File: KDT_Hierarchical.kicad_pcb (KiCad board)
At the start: 2 copper layers, 34 x 40 mm, 33 parts, among them J1 22-28-8083, J2 1x3 pin vertical, J3 1x3 pin vertical, J4 1x3 pin vertical, J5 1x3 pin vertical, P1 5KEV-0, P2 5KEV-0, T1 NSI50010YT1G, U1 INA226

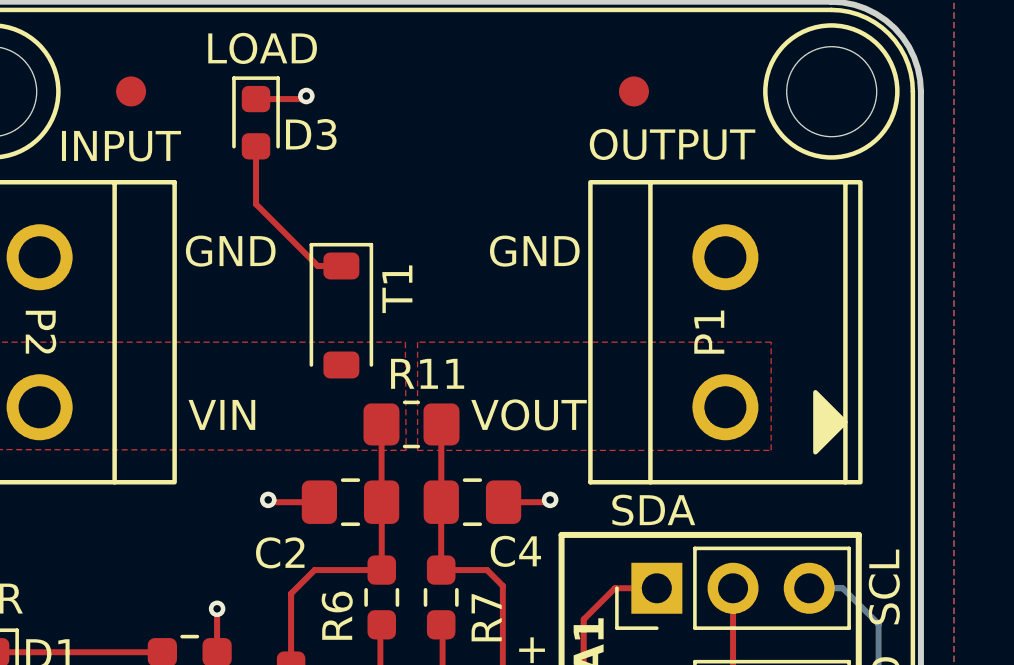
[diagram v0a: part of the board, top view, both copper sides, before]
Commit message: Changed sense resistor and fixed connector position
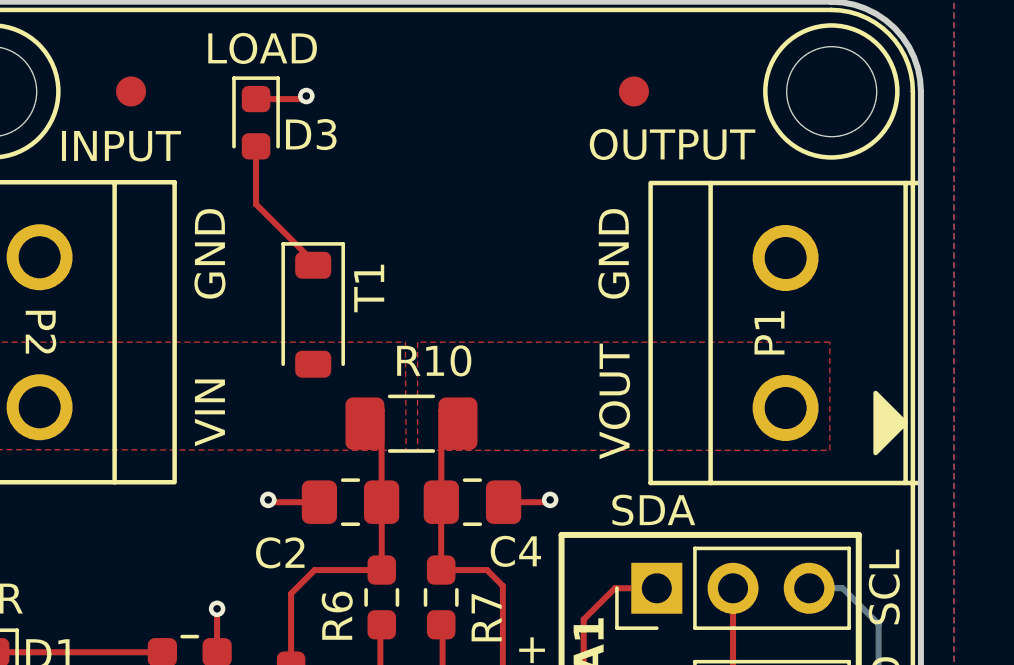
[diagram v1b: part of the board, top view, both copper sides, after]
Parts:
- removed R11: 0.002R, Resistor_SMD:R_0805_2012Metric_Pad1.20x1.40mm_HandSolder
- added R10: 0.002, Resistor_SMD:R_1206_3216Metric_Pad1.30x1.75mm_HandSolder, F.Cu at (130.5, 99.1)
- moved P1 2.01 mm to (143.0, 96.0)
- moved T1 0.94 mm to (127.2, 95.4)
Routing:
- net Net-(D3-A): track 5.63 -> 4.84 mm

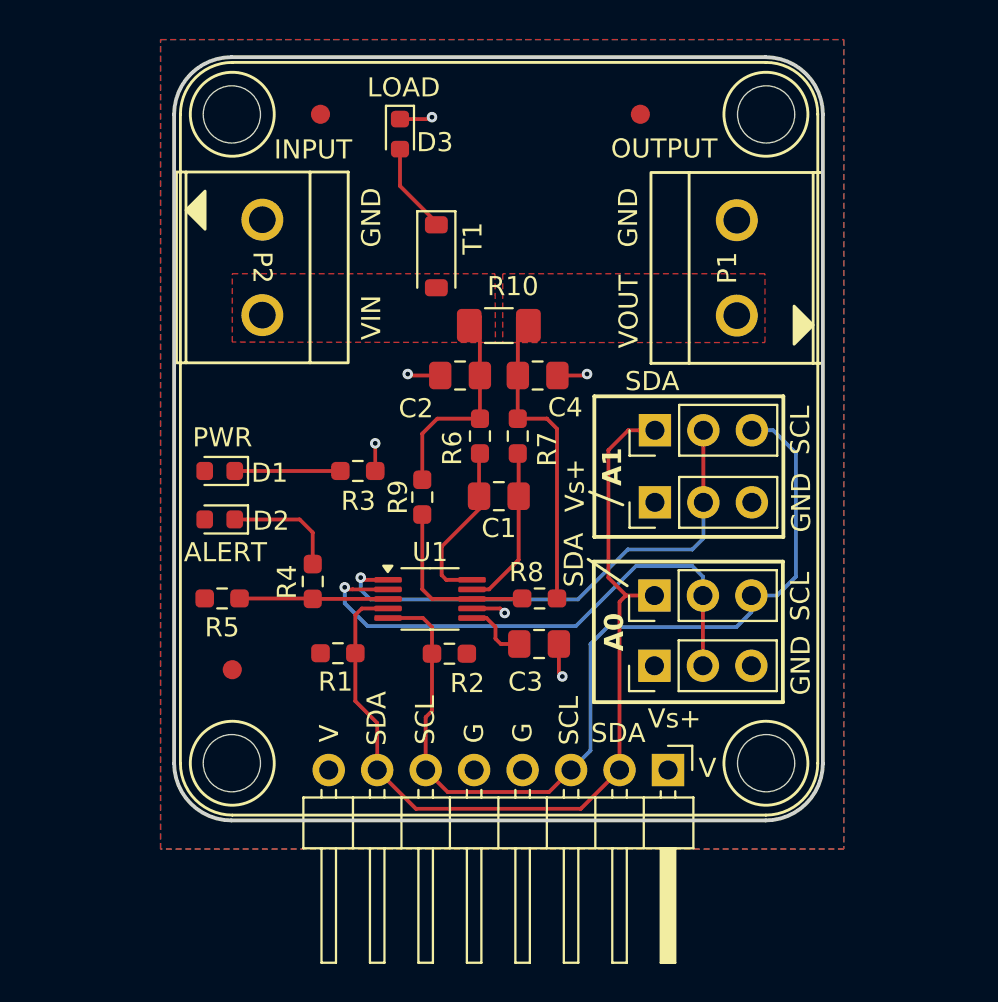
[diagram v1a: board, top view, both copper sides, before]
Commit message: Changed resistor position
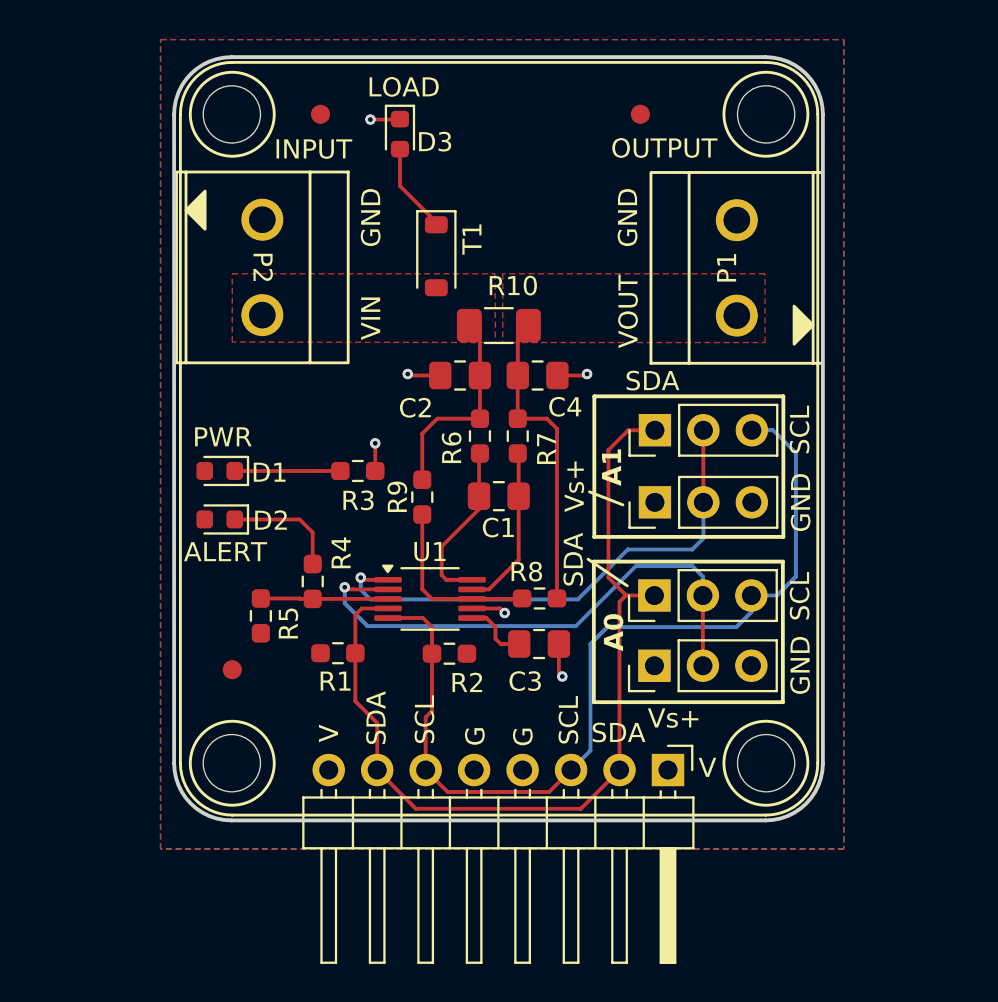
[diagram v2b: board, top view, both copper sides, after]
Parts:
- moved R5 2.23 mm to (118.0, 114.3), turned to 90 degrees
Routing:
- net /Project Architecture/Sense/ALERT: track 7.79 -> 6.71 mm
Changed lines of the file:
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@@
 		(tags "resistor handsolder")
 		(property "Reference" "R4"
-			(at 0.0254 1.3462 90)
+			(at -1.4732 -1.524 90)
 			(layer "F.SilkS")
 			(effects
@@
 	(footprint "Resistor_SMD:R_0603_1608Metric_Pad0.98x0.95mm_HandSolder"
 		(layer "F.Cu")
-		(at 116.0018 113.3602)
+		(at 118.0338 114.2746 90)
 		(descr "Resistor SMD 0603 (1608 Metric), square (rectangular) end terminal, IPC_7351 nominal with elongated pad for handsoldering. (Body size source: IPC-SM-782 page 72, https://www.pcb-3d.com/wordpress/wp-content/uploads/ipc-sm-782a_amendment_1_and_2.pdf), generated with kicad-footprint-generator")
 		(tags "resistor handsolder")
 		(property "Reference" "R5"
-			(at 0 1.524 0)
+			(at -0.4064 1.4732 90)
 			(layer "F.SilkS")
 			(effects
@@
 		)
 		(property "Value" "10K"
-			(at 0 1.43 0)
+			(at 0 1.43 90)
 			(layer "F.Fab")
 			(effects
@@
 		)
 		(property "Datasheet" "https://www.vishay.com/doc?20035"
-			(at 0 0 0)
+			(at 0 0 90)
 			(unlocked yes)
 			(layer "F.Fab")
@@
 		)
 		(property "Description" "RESISTOR, 10K, 5%, 1/10W 0603"
-			(at 0 0 0)
+			(at 0 0 90)
 			(unlocked yes)
 			(layer "F.Fab")
@@
 		)
 		(property "Sim.Device" "R"
-			(at 0 0 0)
+			(at 0 0 90)
 			(unlocked yes)
 			(layer "F.Fab")
@@
 		)
 		(property "Sim.Pins" "1=+ 2=-"
-			(at 0 0 0)
+			(at 0 0 90)
 			(unlocked yes)
 			(layer "F.Fab")
@@
 		)
 		(property "Sim.Params" "r=33"
-			(at 0 0 0)
+			(at 0 0 90)
 			(unlocked yes)
 			(layer "F.Fab")
@@
 		)
 		(property "CompanyPN" "T-RES-004"
-			(at 0 0 0)
+			(at 0 0 90)
 			(unlocked yes)
 			(layer "F.Fab")
@@
 		)
 		(property "Manufacturer Part Number" "CRCW060333R0FKEA"
-			(at 0 0 0)
+			(at 0 0 90)
 			(unlocked yes)
 			(layer "F.Fab")
@@
 		)
 		(fp_line
-			(start -1.65 -0.73)
-			(end 1.65 -0.73)
+			(start 1.65 -0.73)
+			(end 1.65 0.73)
 			(stroke
 				(width 0.05)
@@
 		)
 		(fp_line
-			(start -1.65 0.73)
-			(end -1.65 -0.73)
+			(start -1.65 -0.73)
+			(end 1.65 -0.73)
 			(stroke
 				(width 0.05)
@@
 		)
 		(fp_line
-			(start 1.65 -0.73)
-			(end 1.65 0.73)
+			(start 1.65 0.73)
+			(end -1.65 0.73)
 			(stroke
 				(width 0.05)
@@
 		)
 		(fp_line
-			(start 1.65 0.73)
-			(end -1.65 0.73)
+			(start -1.65 0.73)
+			(end -1.65 -0.73)
 			(stroke
 				(width 0.05)
@@
 		)
 		(fp_line
-			(start -0.8 -0.4125)
-			(end 0.8 -0.4125)
+			(start 0.8 -0.4125)
+			(end 0.8 0.4125)
 			(stroke
 				(width 0.1)
@@
 		)
 		(fp_line
-			(start -0.8 0.4125)
-			(end -0.8 -0.4125)
+			(start -0.8 -0.4125)
+			(end 0.8 -0.4125)
 			(stroke
 				(width 0.1)
@@
 		)
 		(fp_line
-			(start 0.8 -0.4125)
-			(end 0.8 0.4125)
+			(start 0.8 0.4125)
+			(end -0.8 0.4125)
 			(stroke
 				(width 0.1)
@@
 		)
 		(fp_line
-			(start 0.8 0.4125)
-			(end -0.8 0.4125)
+			(start -0.8 0.4125)
+			(end -0.8 -0.4125)
 			(stroke
 				(width 0.1)
@@
 		)
 		(fp_text user "${REFERENCE}"
-			(at 0 0 0)
+			(at 0 0 90)
 			(layer "F.Fab")
 			(effects
@@
 		)
 		(pad "1" smd roundrect
-			(at -0.9125 0)
+			(at -0.9125 0 90)
 			(size 0.975 0.95)
 			(layers "F.Cu" "F.Mask" "F.Paste")
@@
 		)
 		(pad "2" smd roundrect
-			(at 0.9125 0)
+			(at 0.9125 0 90)
 			(size 0.975 0.95)
 			(layers "F.Cu" "F.Mask" "F.Paste")
@@
 	)
 	(gr_text "G"
-		(at 132.334 120.9294 90)
+		(at 132.3848 121.1326 90)
 		(layer "F.SilkS")
 		(effects
@@
 	)
 	(gr_text "G"
-		(at 129.794 120.9548 90)
+		(at 129.8702 121.1072 90)
 		(layer "F.SilkS")
 		(effects
@@
 	)
 	(segment
-		(start 125.3236 88.2395)
-		(end 126.8985 88.2395)
+		(start 124.0263 106.68)
+		(end 124.0263 105.2303)
 		(width 0.2)
 		(layer "F.Cu")
@@
 	)
 	(segment
-		(start 124.0263 106.68)
-		(end 124.0263 105.2303)
+		(start 133.6509 115.7478)
+		(end 133.6509 117.2679)
 		(width 0.2)
 		(layer "F.Cu")
@@
 	)
 	(segment
-		(start 133.6509 115.7478)
-		(end 133.6509 117.2679)
+		(start 125.2981 88.265)
+		(end 125.3236 88.2395)
 		(width 0.2)
 		(layer "F.Cu")
@@
 	)
 	(segment
-		(start 126.8985 88.2395)
-		(end 127 88.138)
+		(start 123.7742 88.265)
+		(end 125.2981 88.265)
 		(width 0.2)
 		(layer "F.Cu")
@@
 	)
 	(via
-		(at 127 88.138)
+		(at 123.7742 88.265)
 		(size 0.55)
 		(drill 0.25)
@@
 	)
 	(segment
-		(start 116.9143 113.3602)
-		(end 120.7281 113.3602)
+		(start 120.0715 113.3621)
+		(end 118.0338 113.3621)
 		(width 0.2)
 		(layer "F.Cu")
@@
 	)
 	(segment
+		(start 120.0931 113.3837)
+		(end 120.0715 113.3621)
+		(width 0.2)
+		(layer "F.Cu")
+		(net 14)
+	)
+	(segment
 		(start 124.0517 113.3837)
 		(end 120.7516 113.3837)
 		(width 0.2)
 		(layer "F.Cu")
+		(net 14)
+	)
+	(segment
+		(start 120.7516 113.3837)
+		(end 120.0931 113.3837)
+		(width 0.2)
+		(layer "F.Cu")

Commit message: Split I2C connector
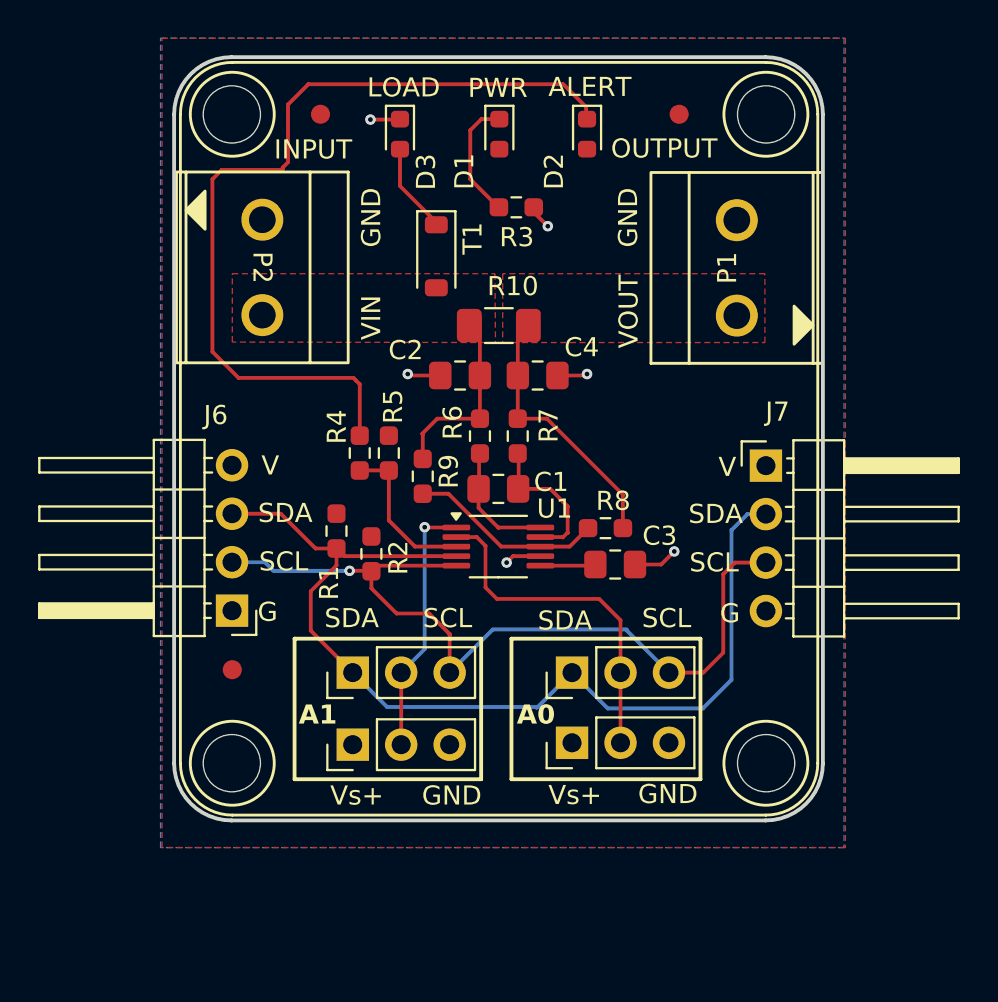
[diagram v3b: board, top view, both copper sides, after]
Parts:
- removed J1: 22-28-8083, Connector_PinHeader_2.54mm:PinHeader_1x08_P2.54mm_Horizontal
- added J6: 22-28-6040, Connector_PinHeader_2.54mm:PinHeader_1x04_P2.54mm_Horizontal, F.Cu at (116.5, 114.0)
- added J7: 22-28-6040, Connector_PinHeader_2.54mm:PinHeader_1x04_P2.54mm_Horizontal, F.Cu at (144.5, 106.4)
- moved D2 27.9 mm to (135.1, 89.0), turned to -90 degrees
- moved D1 22.9 mm to (130.5, 89.0), turned to -90 degrees
- moved J4 20.3 mm to (122.8, 121.0)
- moved J5 20.3 mm to (122.8, 117.2)
- moved R3 16.1 mm to (131.4, 92.9)
- moved R5 10.9 mm to (124.7, 105.7), turned to -90 degrees
- moved R4 7.17 mm to (123.2, 105.7)
- moved R2 6.64 mm to (123.8, 111.0), turned to -90 degrees
- moved R1 6.40 mm to (122.0, 109.8), turned to -90 degrees
- moved J2 5.91 mm to (134.3, 120.9)
- moved J3 5.91 mm to (134.3, 117.2)
- moved C3 5.77 mm to (136.6, 111.6)
- moved R8 5.05 mm to (136.1, 109.7)
- moved U1 4.51 mm to (130.5, 110.6)
- moved FID1 2.03 mm to (140.0, 88.0)
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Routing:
- net Net-(D2-K): track 6.00 -> 44.8 mm
- net /Project Architecture/Sense/A1: track 27.3 -> 13.6 mm
- net /Project Architecture/Sense/A0: track 28.6 -> 18.1 mm, vias 1 -> 0
- net /Project Architecture/Sense/SDA: track 45.7 -> 53.4 mm
- net /Project Architecture/Sense/SCL: track 47.3 -> 43.3 mm, vias 0 -> 1
- net /Project Architecture/Sense/VIN-: track 16.5 -> 14.3 mm
- net /Project Architecture/Sense/VIN+INA: track 8.90 -> 6.92 mm
- net /Project Architecture/Sense/ALERT: track 6.71 -> 8.25 mm
- net /Project Architecture/Sense/VIN+: track 11.1 -> 10.0 mm
- net Net-(D1-K): track 5.57 -> 6.48 mm
- net VBUS: track 9.47 -> 10.2 mm
- net GND: track 9.77 -> 10.4 mm
- net /Project Architecture/Sense/VIN-INA: track 8.68 -> 8.16 mm
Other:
- board text added: "0.07mm (2oz)"
- board text added: "1.48mm"
- board text removed: "???mm"
- board text removed: "???mm (?oz)"
- board text removed: "L3 (Sig, PWR)"
- board text removed: "L4 (Sig, PWR)"
- board text removed: "L5 (GND)"
- board text removed: "L6 (Sig, PWR)"
- board text removed: "Prepreg"

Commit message: Outputs generated, ready for prototyping
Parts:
- added TP1: TestPoint, 0_testpoints:TestPoint_PTH_1mm_2mm, B.Cu at (135.2, 106.3)
- added TP2: TestPoint, 0_testpoints:TestPoint_PTH_1mm_2mm, B.Cu at (138.4, 102.9)
- added TP3: TestPoint, 0_testpoints:TestPoint_PTH_1mm_2mm, B.Cu at (134.8, 93.4)
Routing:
- net VBUS: track 10.2 -> 13.6 mm
- net /Project Architecture/Sense/VIN-: track 14.3 -> 16.1 mm
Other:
- board text added: "0 0 0"
- board text added: "18.726 22.054 31.630"
- board text added: "21.704 22.854 21.349"
- board text added: "8 17 25"
- board text added: "TP1 TP2 TP3"
- board text added: "VBUS VCC GND"
- board text removed: "??? ??? ???"
- board text removed: "??? ??? ??? ??? ??? (slot) ??? ??? ??? ??? ???"
- board text removed: "???mm ???mm ???mm ???mm ???mm ???mm ???mm ???mm ???mm ???mm"
- board text removed: "Plated Plated Plated Plated Plated Plated Plated Plated Plated Unplated"
- board text removed: "TP? TP? TP?"

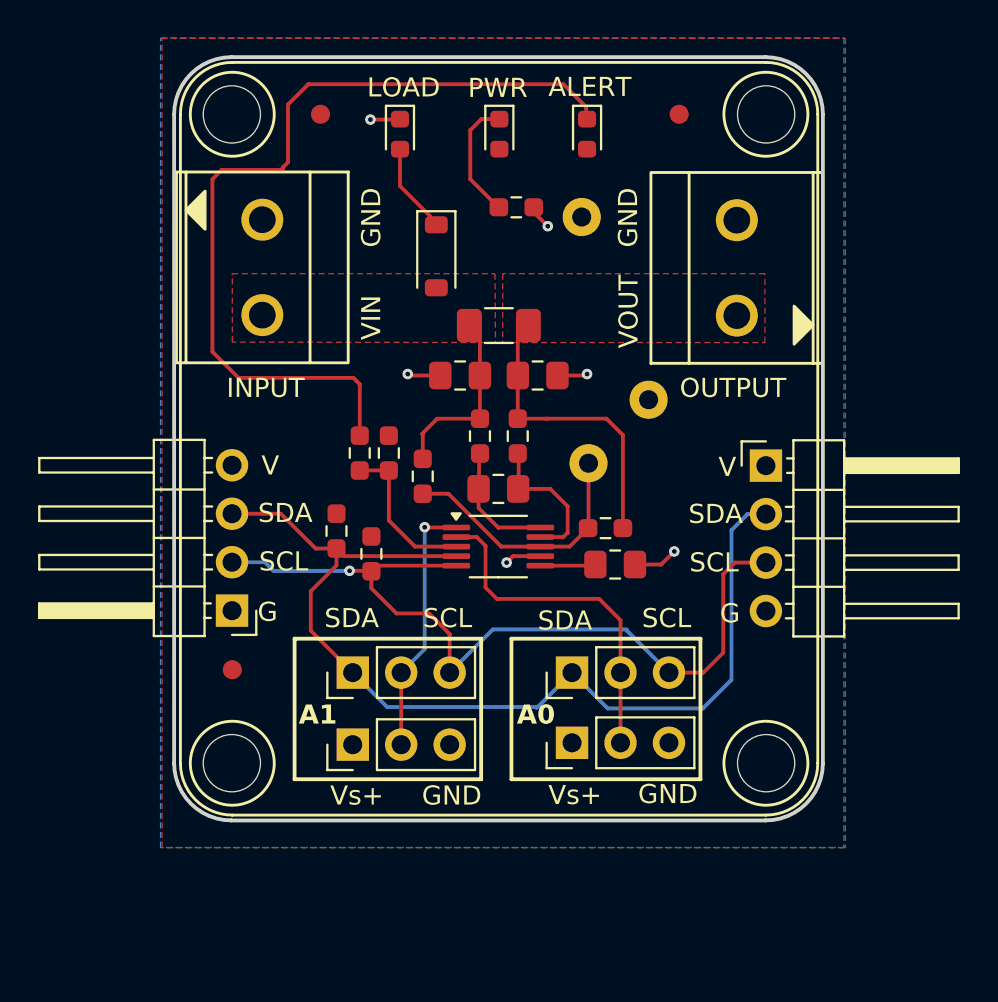
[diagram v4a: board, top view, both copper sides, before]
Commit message: fixed component positions
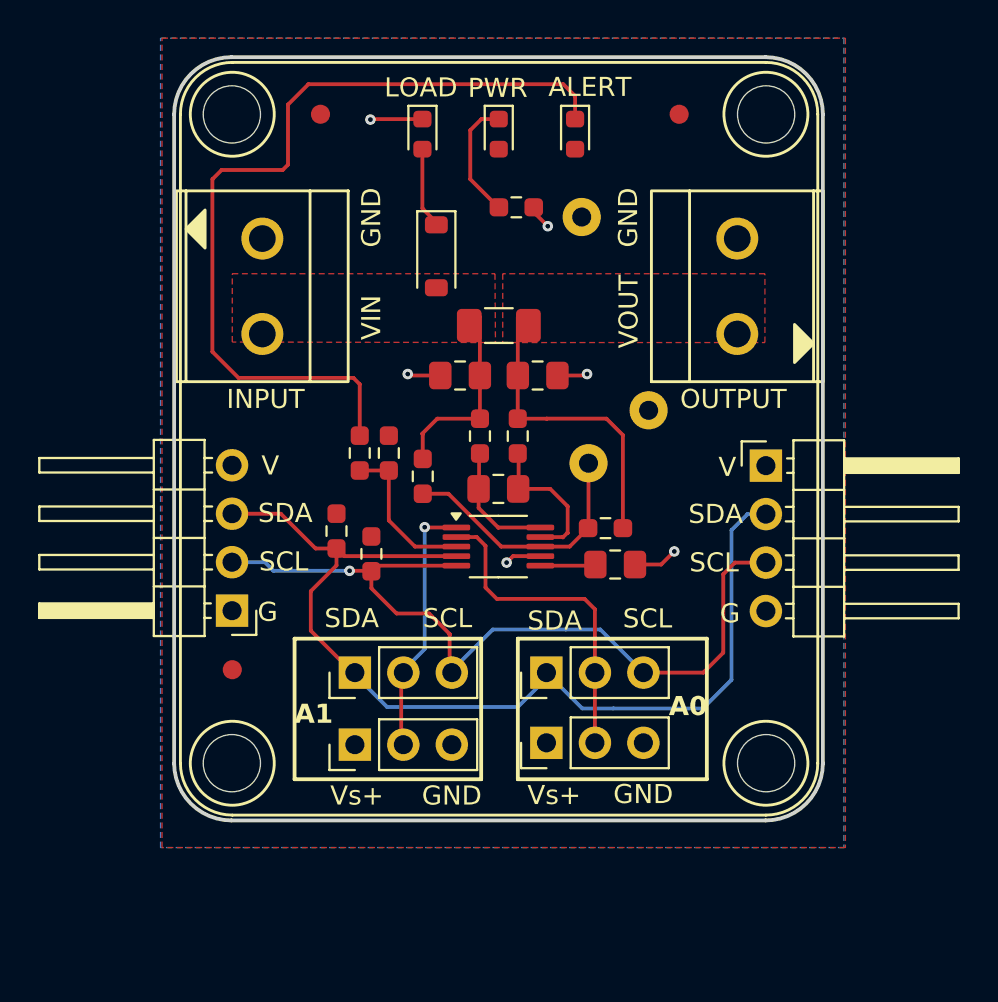
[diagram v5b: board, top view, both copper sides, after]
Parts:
- moved J2 1.34 mm to (133.0, 120.9)
- moved J3 1.34 mm to (133.0, 117.2)
- moved D3 1.18 mm to (126.5, 89.0)
- moved P2 0.99 mm to (118.1, 97.0)
- moved P1 0.96 mm to (143.0, 97.0)
- moved D2 0.63 mm to (134.5, 89.0)
- moved TP2 0.55 mm to (138.4, 103.5)
- moved J4 0.11 mm to (123.0, 121.0)
- moved J5 0.11 mm to (123.0, 117.2)
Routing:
- net GND: track 10.4 -> 11.6 mm
- net /Project Architecture/Sense/A0: track 18.1 -> 17.1 mm
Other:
- board text added: "18.726 21.500 31.630"
- board text added: "21.704 24.850 21.349"
- board text removed: "18.726 22.054 31.630"
- board text removed: "21.704 22.854 21.349"
- board text removed: "Count"
- board text removed: "Hole Size"
- board text removed: "Plated"
- board text removed: "Symbol"
